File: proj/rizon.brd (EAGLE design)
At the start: 100 x 80 mm, 27 parts, among them J1 PWRJACK5521, U1 Z8400, U2 AS6C62256PDIP, U3 AS6C62256PDIP, U4 AT28C64BPLCC, U5 AT28C64BPLCC, U6 7432PDIP, U7 7805TO220, U8 7432PDIP, U9 7400PDIP, X1 OSC412.7

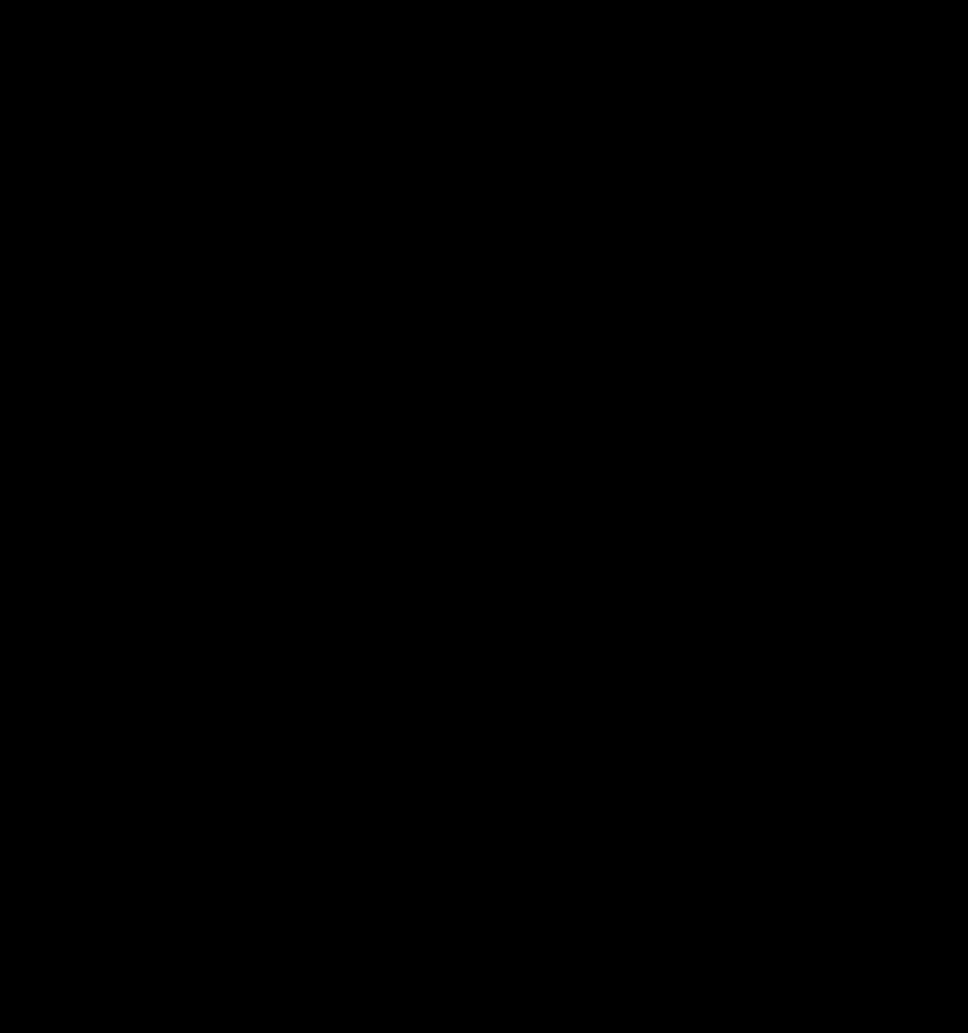
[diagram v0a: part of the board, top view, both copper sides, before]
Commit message: Added 74374 to library Further designed Rizon Z80 SBC
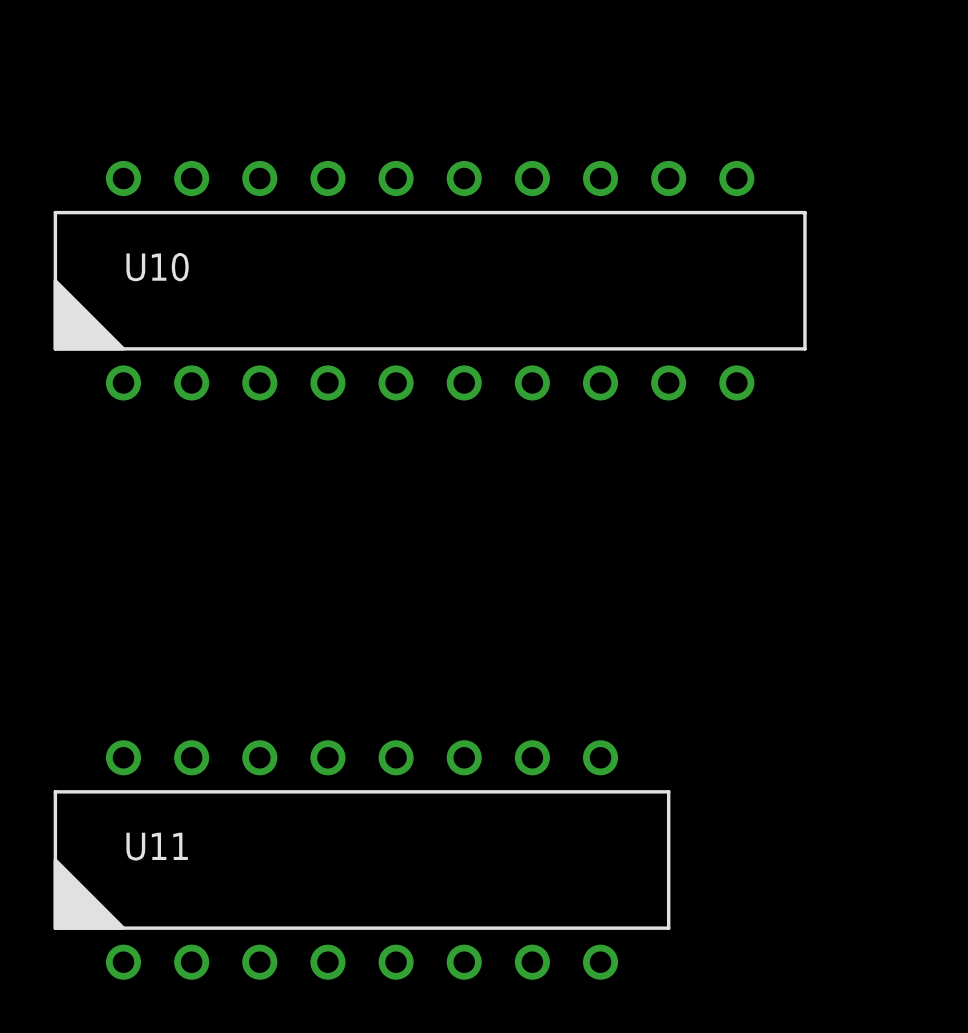
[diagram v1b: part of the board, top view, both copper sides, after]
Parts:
- added U10: 74374PDIP, dooba:PDIP20
- added U11: 74138PDIP, dooba:PDIP16
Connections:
- net !RAM_BANK1_CE renamed !HIGH_ADDR
- net !ROM_BANK1_CE renamed !ROM_BANK1
- removed net N$6: U1.31
- new net !INT: U1.18
- new net !IODEV0: U11.P$15
- new net !IODEV1: U11.P$14
- new net !IODEV2: U11.P$13
- new net !IODEV3: U11.P$12
- new net !IODEV4: U11.P$11
- new net !IODEV5: U11.P$10
- new net !IODEV6: U11.P$9
- new net !IODEV7: U11.P$7
- new net !M1: U1.31, U11.P$6
- new net !ROM_EN: U10.P$2
- net !IORQ: now also U11.P$4, U11.P$5
- net ADDR0: now also U11.P$1
- net ADDR1: now also U11.P$2
- net ADDR2: now also U11.P$3
- net DATA0: now also U10.P$3
- net DATA1: now also U10.P$4
- net DATA2: now also U10.P$7
- net DATA3: now also U10.P$8
- net DATA4: now also U10.P$13
- net DATA5: now also U10.P$14
- net DATA6: now also U10.P$17
- net DATA7: now also U10.P$18
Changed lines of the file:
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@@
 <element name="X1" library="dooba" package="OSC127" value="OSC412.7" x="-71.12" y="57.15"/>
 <element name="U9" library="dooba" package="PDIP14" value="7400PDIP" x="-72.39" y="-13.97"/>
+<element name="U10" library="dooba" package="PDIP20" value="74374PDIP" x="-68.58" y="-35.56"/>
+<element name="U11" library="dooba" package="PDIP16" value="74138PDIP" x="-71.12" y="-57.15"/>
 </elements>
 <signals>
@@
 <signal name="DATA1">
 <contactref element="U1" pad="17"/>
+<contactref element="U10" pad="P$4"/>
+<wire x1="-34.29" y1="6.35" x2="-72.39" y2="-39.37" width="0" layer="19" extent="1-1"/>
 </signal>
 <signal name="DATA0">
 <contactref element="U1" pad="16"/>
+<contactref element="U10" pad="P$3"/>
+<wire x1="-31.75" y1="8.89" x2="-74.93" y2="-39.37" width="0" layer="19" extent="1-1"/>
 </signal>
 <signal name="DATA7">
 <contactref element="U1" pad="15"/>
+<contactref element="U10" pad="P$18"/>
+<wire x1="-34.29" y1="8.89" x2="-74.93" y2="-31.75" width="0" layer="19" extent="1-1"/>
 </signal>
 <signal name="DATA2">
 <contactref element="U1" pad="14"/>
+<contactref element="U10" pad="P$7"/>
+<wire x1="-31.75" y1="11.43" x2="-64.77" y2="-39.37" width="0" layer="19" extent="1-1"/>
 </signal>
 <signal name="DATA6">
 <contactref element="U1" pad="11"/>
+<contactref element="U10" pad="P$17"/>
+<wire x1="-34.29" y1="13.97" x2="-72.39" y2="-31.75" width="0" layer="19" extent="1-1"/>
 </signal>
 <signal name="DATA5">
 <contactref element="U1" pad="10"/>
+<contactref element="U10" pad="P$14"/>
+<wire x1="-31.75" y1="16.51" x2="-64.77" y2="-31.75" width="0" layer="19" extent="1-1"/>
 </signal>
 <signal name="DATA3">
 <contactref element="U1" pad="9"/>
+<contactref element="U10" pad="P$8"/>
+<wire x1="-34.29" y1="16.51" x2="-62.23" y2="-39.37" width="0" layer="19" extent="1-1"/>
 </signal>
 <signal name="DATA4">
 <contactref element="U1" pad="8"/>
+<contactref element="U10" pad="P$13"/>
+<wire x1="-31.75" y1="19.05" x2="-62.23" y2="-31.75" width="0" layer="19" extent="1-1"/>
 </signal>
 <signal name="ADDR15">
@@
 <contactref element="U4" pad="9"/>
 <contactref element="U5" pad="9"/>
+<contactref element="U11" pad="P$3"/>
+<wire x1="-58.42" y1="11.43" x2="-74.93" y2="-60.96" width="0" layer="19" extent="1-1"/>
 <wire x1="-55.88" y1="29.21" x2="-58.42" y2="11.43" width="0" layer="19" extent="1-1"/>
 <wire x1="-34.29" y1="38.1" x2="-55.88" y2="29.21" width="0" layer="19" extent="1-1"/>
@@
 <contactref element="U4" pad="10"/>
 <contactref element="U5" pad="10"/>
+<contactref element="U11" pad="P$2"/>
+<wire x1="-55.88" y1="11.43" x2="-77.47" y2="-60.96" width="0" layer="19" extent="1-1"/>
 <wire x1="-53.34" y1="29.21" x2="-55.88" y2="11.43" width="0" layer="19" extent="1-1"/>
 <wire x1="-31.75" y1="38.1" x2="-53.34" y2="29.21" width="0" layer="19" extent="1-1"/>
@@
 <contactref element="U4" pad="11"/>
 <contactref element="U5" pad="11"/>
+<contactref element="U11" pad="P$1"/>
+<wire x1="-58.42" y1="8.89" x2="-80.01" y2="-60.96" width="0" layer="19" extent="1-1"/>
 <wire x1="-50.8" y1="29.21" x2="-58.42" y2="8.89" width="0" layer="19" extent="1-1"/>
 <wire x1="-34.29" y1="35.56" x2="-50.8" y2="29.21" width="0" layer="19" extent="1-1"/>
@@
 <signal name="!IORQ">
 <contactref element="U1" pad="22"/>
+<contactref element="U11" pad="P$4"/>
+<contactref element="U11" pad="P$5"/>
+<wire x1="-69.85" y1="-60.96" x2="-72.39" y2="-60.96" width="0" layer="19" extent="1-1"/>
+<wire x1="-26.67" y1="3.81" x2="-69.85" y2="-60.96" width="0" layer="19" extent="1-1"/>
 </signal>
 <signal name="!RD">
@@
 <contactref element="U1" pad="20"/>
 </signal>
-<signal name="N$6">
+<signal name="!M1">
 <contactref element="U1" pad="31"/>
-</signal>
-<signal name="!RAM_BANK1_CE">
+<contactref element="U11" pad="P$6"/>
+<wire x1="-16.51" y1="8.89" x2="-67.31" y2="-60.96" width="0" layer="19" extent="1-1"/>
+</signal>
+<signal name="!HIGH_ADDR">
 <contactref element="U9" pad="P$3"/>
 </signal>
@@
 <contactref element="U9" pad="P$8"/>
 </signal>
-<signal name="!ROM_BANK1_CE">
+<signal name="!ROM_BANK1">
 <contactref element="U9" pad="P$6"/>
 </signal>
+<signal name="!INT">
+<contactref element="U1" pad="18"/>
+</signal>
+<signal name="!IODEV0">
+<contactref element="U11" pad="P$15"/>
+</signal>
+<signal name="!IODEV1">
+<contactref element="U11" pad="P$14"/>
+</signal>
+<signal name="!IODEV2">
+<contactref element="U11" pad="P$13"/>
+</signal>
+<signal name="!IODEV3">
+<contactref element="U11" pad="P$12"/>
+</signal>
+<signal name="!IODEV4">
+<contactref element="U11" pad="P$11"/>
+</signal>
+<signal name="!IODEV5">
+<contactref element="U11" pad="P$10"/>
+</signal>
+<signal name="!IODEV6">
+<contactref element="U11" pad="P$9"/>
+</signal>
+<signal name="!IODEV7">
+<contactref element="U11" pad="P$7"/>
+</signal>
+<signal name="!ROM_EN">
+<contactref element="U10" pad="P$2"/>
+</signal>
 </signals>

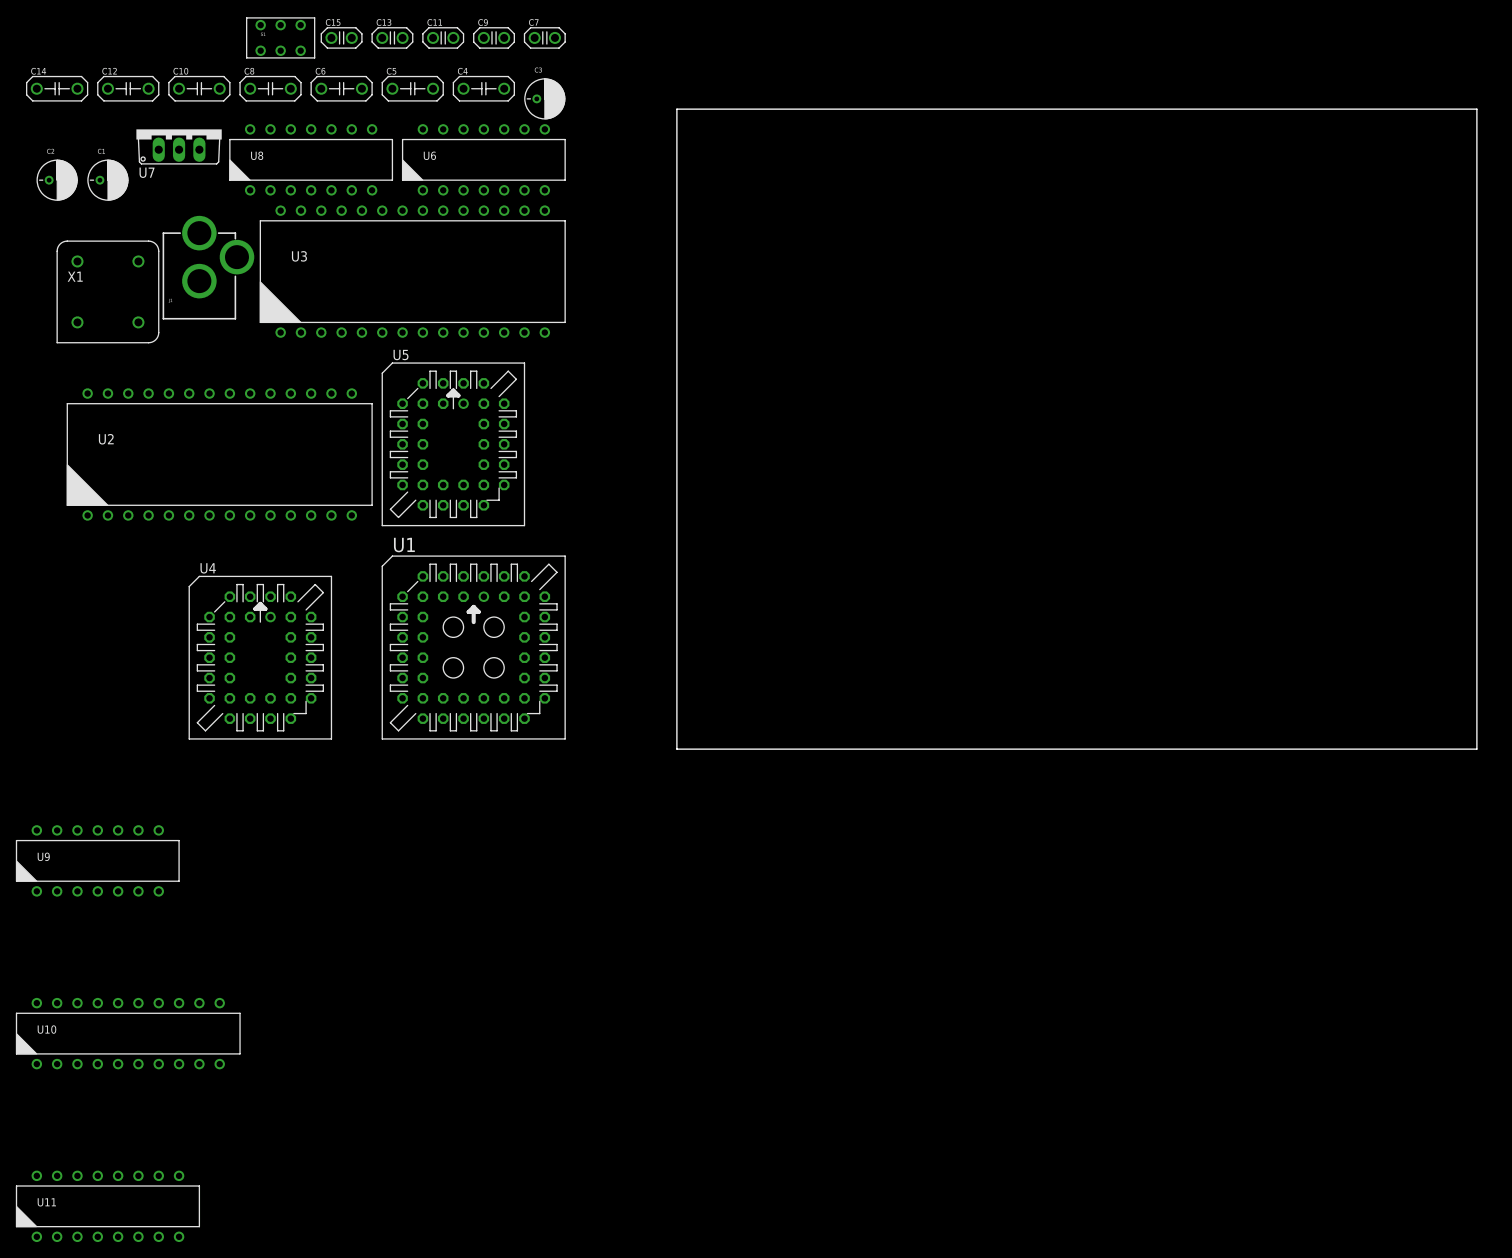
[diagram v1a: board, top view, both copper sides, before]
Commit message: Started designing main board for Rizon Z80 computer
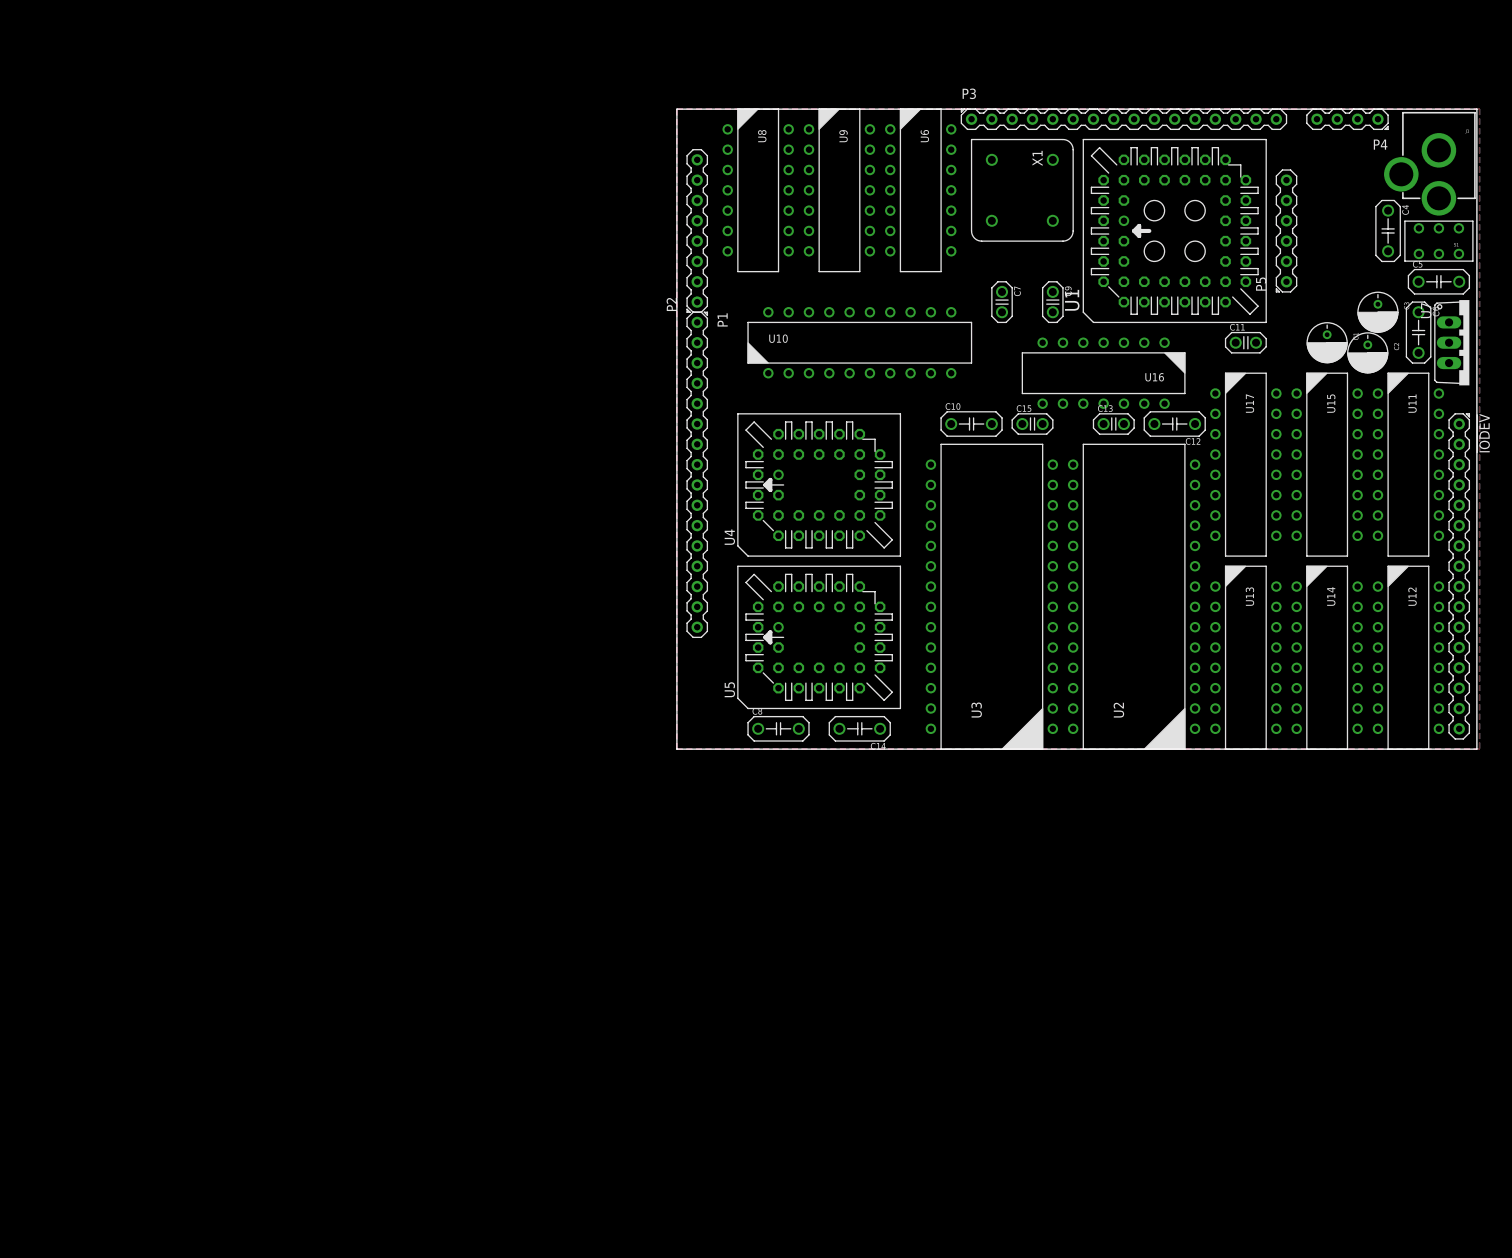
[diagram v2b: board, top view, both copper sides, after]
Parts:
- added !IODEV, P1: ADDR, dooba:PIN_16
- added P2: DATA, dooba:PIN_8
- added P3: CTL, dooba:PIN_16
- added P4: PWR, dooba:PIN_4
- added P5: 10k, dooba:PIN_6
- added U12, U13, U14, U15, U17: 74138PDIP, dooba:PDIP16
- added U16: 7432PDIP, dooba:PDIP14
- U10: value 74374PDIP -> 74273PDIP
- moved U11 187.1 mm to (91.4, 35.6), turned to 270 degrees
- moved C2 165.2 mm to (86.4, 49.5), turned to 270 degrees
- moved U7 163.5 mm to (99.1, 50.8), turned to 270 degrees
- moved J1 155.8 mm to (95.2, 74.9), turned to 180 degrees
- moved C1 153.7 mm to (81.3, 50.8), turned to 270 degrees
- moved S1 147.0 mm to (95.2, 63.5), turned to 180 degrees
- moved C6 138.0 mm to (92.7, 52.1), turned to 270 degrees
- moved C12 137.4 mm to (62.2, 40.6), turned to 180 degrees
- moved C5 130.5 mm to (95.2, 58.4)
- moved C14 128.3 mm to (22.9, 2.54), turned to 180 degrees
- moved U10 125.8 mm to (22.9, 50.8)
- moved U9 125.0 mm to (20.3, 69.8), turned to 270 degrees
- moved U2 115.7 mm to (57.1, 19.1), turned to 90 degrees
- moved X1 115.0 mm to (43.2, 69.8), turned to 270 degrees
- moved C4 114.4 mm to (88.9, 64.8), turned to 270 degrees
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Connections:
- removed net !ROM_EN: U10.P$2
- removed net N$7: U9.P$8
- new net !BUSACK: P3.10, U1.27
- new net !BUSREQ: P3.12, P5.6, U1.29
- new net !IODEV10: !IODEV.11, U12.P$13
- new net !IODEV11: !IODEV.12, U12.P$12
- new net !IODEV12: !IODEV.13, U12.P$11
- new net !IODEV13: !IODEV.14, U12.P$10
- new net !IODEV14: !IODEV.15, U12.P$9
- new net !IODEV15: !IODEV.16, U12.P$7
- new net !IODEV8: !IODEV.9, U12.P$15
- new net !IODEV9: !IODEV.10, U12.P$14
- new net !IO_SELECT_BANK0: U11.P$5, U13.P$15
- new net !IO_SELECT_BANK1: U12.P$5, U13.P$14
- new net !MEM_SELECT_LOWRAM: U6.P$6, U8.P$1
- new net !MEM_SELECT_ROM: U6.P$10, U6.P$13, U6.P$3
- new net !MEM_SELECT_ROM_BANK0: U6.P$8, U8.P$9
- new net !MEM_SELECT_ROM_BANK1: U6.P$11, U8.P$12
- new net !NMI: P3.4, P5.3, U1.19
- new net !RAM_BANK0_CE: U2.P$20, U8.P$3
- new net !RAM_BANK1_CE: U3.P$20, U8.P$6
- new net !RESET: P3.15, P5.4, U1.30, U10.P$1
- new net !RFSH: P3.14, U1.32
- new net !ROM_BANK0_CE: U4.23, U8.P$8
- new net !ROM_BANK1_CE: U5.23, U8.P$11
- new net !SCR0_CP: U16.P$3, U9.P$12, U9.P$13
- new net !SCR0_ROM_EN: U10.P$2, U6.P$2, U9.P$10, U9.P$9
- new net !WAIT: P3.11, P5.5, U1.28
- new net CLK: P3.1, U1.7, X1.5
- new net N$1: U13.P$5, U14.P$15
- new net N$2: U14.P$5, U15.P$15
- new net N$3: U15.P$5, U17.P$15
- new net N$4: J1.PWR, S1.1, S1.4
- new net SCR0_CP: U10.P$11, U9.P$11
- new net SCR0_ROM_EN: U6.P$5, U9.P$8
- new net VCC: C1.+, C10.P$2, C11.P$2, C12.P$2, C13.P$2, C14.P$2, C15.P$2, C2.+, C5.P$2, C6.P$2, C7.P$2, C8.P$2, C9.P$2, P4.4, P5.1, U1.13, U10.P$20, U11.P$16, U12.P$16, U13.P$16, U14.P$16, U15.P$16, U16.P$14, U17.P$16, U2.P$28, U3.P$28, U4.32, U5.32, U6.P$14, U7.3, U8.P$14, U9.P$14, X1.8
- new net VIN: C3.+, C4.P$2, P4.2, S1.2, S1.5, U7.1
- net !HALT: now also P3.5
- net !HIGH_ADDR: now also U8.P$4
- net !INT: now also P3.3, P5.2
- net !IODEV0: now also U16.P$1
- net !IODEV1: now also !IODEV.2
- net !IODEV2: now also !IODEV.3
- net !IODEV3: now also !IODEV.4
- net !IODEV4: now also !IODEV.5
- net !IODEV5: now also !IODEV.6
- net !IODEV6: now also !IODEV.7
- net !IODEV7: now also !IODEV.8
- net !IORQ: now also P3.7, U12.P$4, U13.P$4, U14.P$4, U15.P$4, U17.P$4; no longer U11.P$5
- net !M1: now also P3.13, U12.P$6, U13.P$6, U14.P$6, U15.P$6, U17.P$6
- net !MREQ: now also P3.6, U8.P$10, U8.P$13, U8.P$2, U8.P$5
- net !RD: now also P3.8, U2.P$22, U3.P$22, U4.25, U5.25
- net !ROM_BANK1: now also U6.P$12
- net !WR: now also P3.9, U16.P$2, U2.P$27, U3.P$27, U4.31, U5.31
- net ADDR0: now also P1.1, U12.P$1
- net ADDR1: now also P1.2, U12.P$2
- net ADDR10: now also P1.11, U15.P$2
- net ADDR11: now also P1.12, U15.P$3
- net ADDR12: now also P1.13, U17.P$1
- net ADDR13: now also P1.14, U17.P$2, U6.P$9
- net ADDR14: now also P1.15, U17.P$3
- net ADDR15: now also P1.16, U17.P$5, U6.P$1, U6.P$4
- net ADDR2: now also P1.3, U12.P$3
- net ADDR3: now also P1.4, U13.P$1
- net ADDR4: now also P1.5, U13.P$2
- net ADDR5: now also P1.6, U13.P$3
- net ADDR6: now also P1.7, U14.P$1
- net ADDR7: now also P1.8, U14.P$2
- net ADDR8: now also P1.9, U14.P$3
- net ADDR9: now also P1.10, U15.P$1
- net DATA0: now also P2.1, U2.P$11, U3.P$11, U4.13, U5.13
- net DATA1: now also P2.2, U2.P$12, U3.P$12, U4.14, U5.14
- net DATA2: now also P2.3, U2.P$13, U3.P$13, U4.15, U5.15
- net DATA3: now also P2.4, U2.P$15, U3.P$15, U4.18, U5.18
- net DATA4: now also P2.5, U2.P$16, U3.P$16, U4.19, U5.19
- net DATA5: now also P2.6, U2.P$17, U3.P$17, U4.20, U5.20
- net DATA6: now also P2.7, U2.P$18, U3.P$18, U4.21, U5.21
- net DATA7: now also P2.8, U2.P$19, U3.P$19, U4.22, U5.22
- net GND: now also !IODEV.1, P3.16, P3.2, P4.1, P4.3, U10.P$10, U11.P$8, U12.P$8, U13.P$8, U14.P$8, U15.P$8, U16.P$7, U17.P$8
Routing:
- added copper zone on layer 1, net GND
- added copper zone on layer 16, net GND
